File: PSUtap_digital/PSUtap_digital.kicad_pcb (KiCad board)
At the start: 2 copper layers, 179.6 x 181.6 mm, 90 parts, among them J1 USB_B_Micro, J2 ADC_board_SPI, J3 SD_card_SPI, J4 Screen_SPI, SW1 Up, SW2 Down, SW3 Left, SW4 Right, SW5 B, SW6 A, SW7 SW_DPST_x2, T1 CTX33-3, U1 LT1512, U2 BQ2973, U3 Si6926ADQ, U4 CH340G, U5 ATmega328P-AU, U6 LTC3525-5, Y1 12MHz, Y2 16MHz

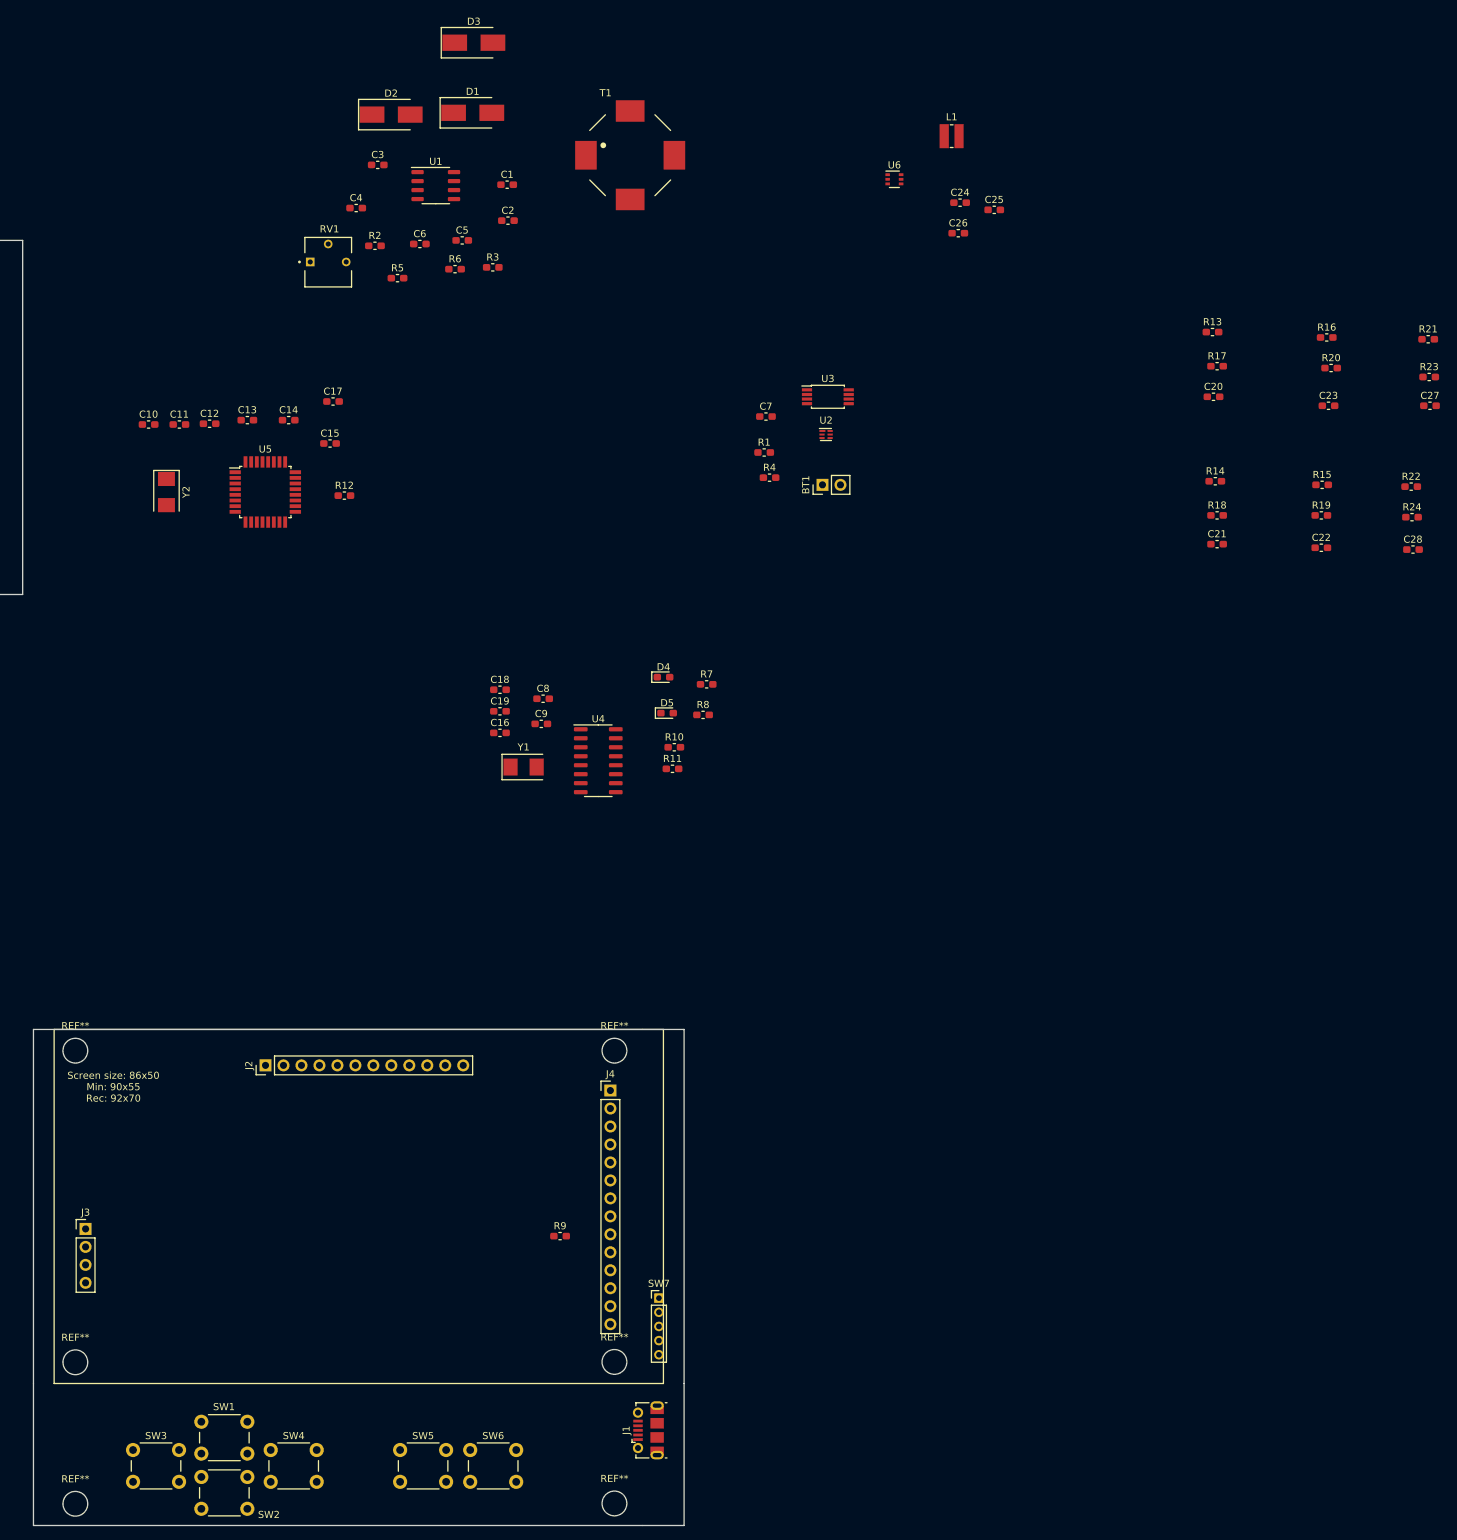
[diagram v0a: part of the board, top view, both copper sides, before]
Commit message: Removed PCB copies, added xtal to ADC in analog board, finished digital board's PCB
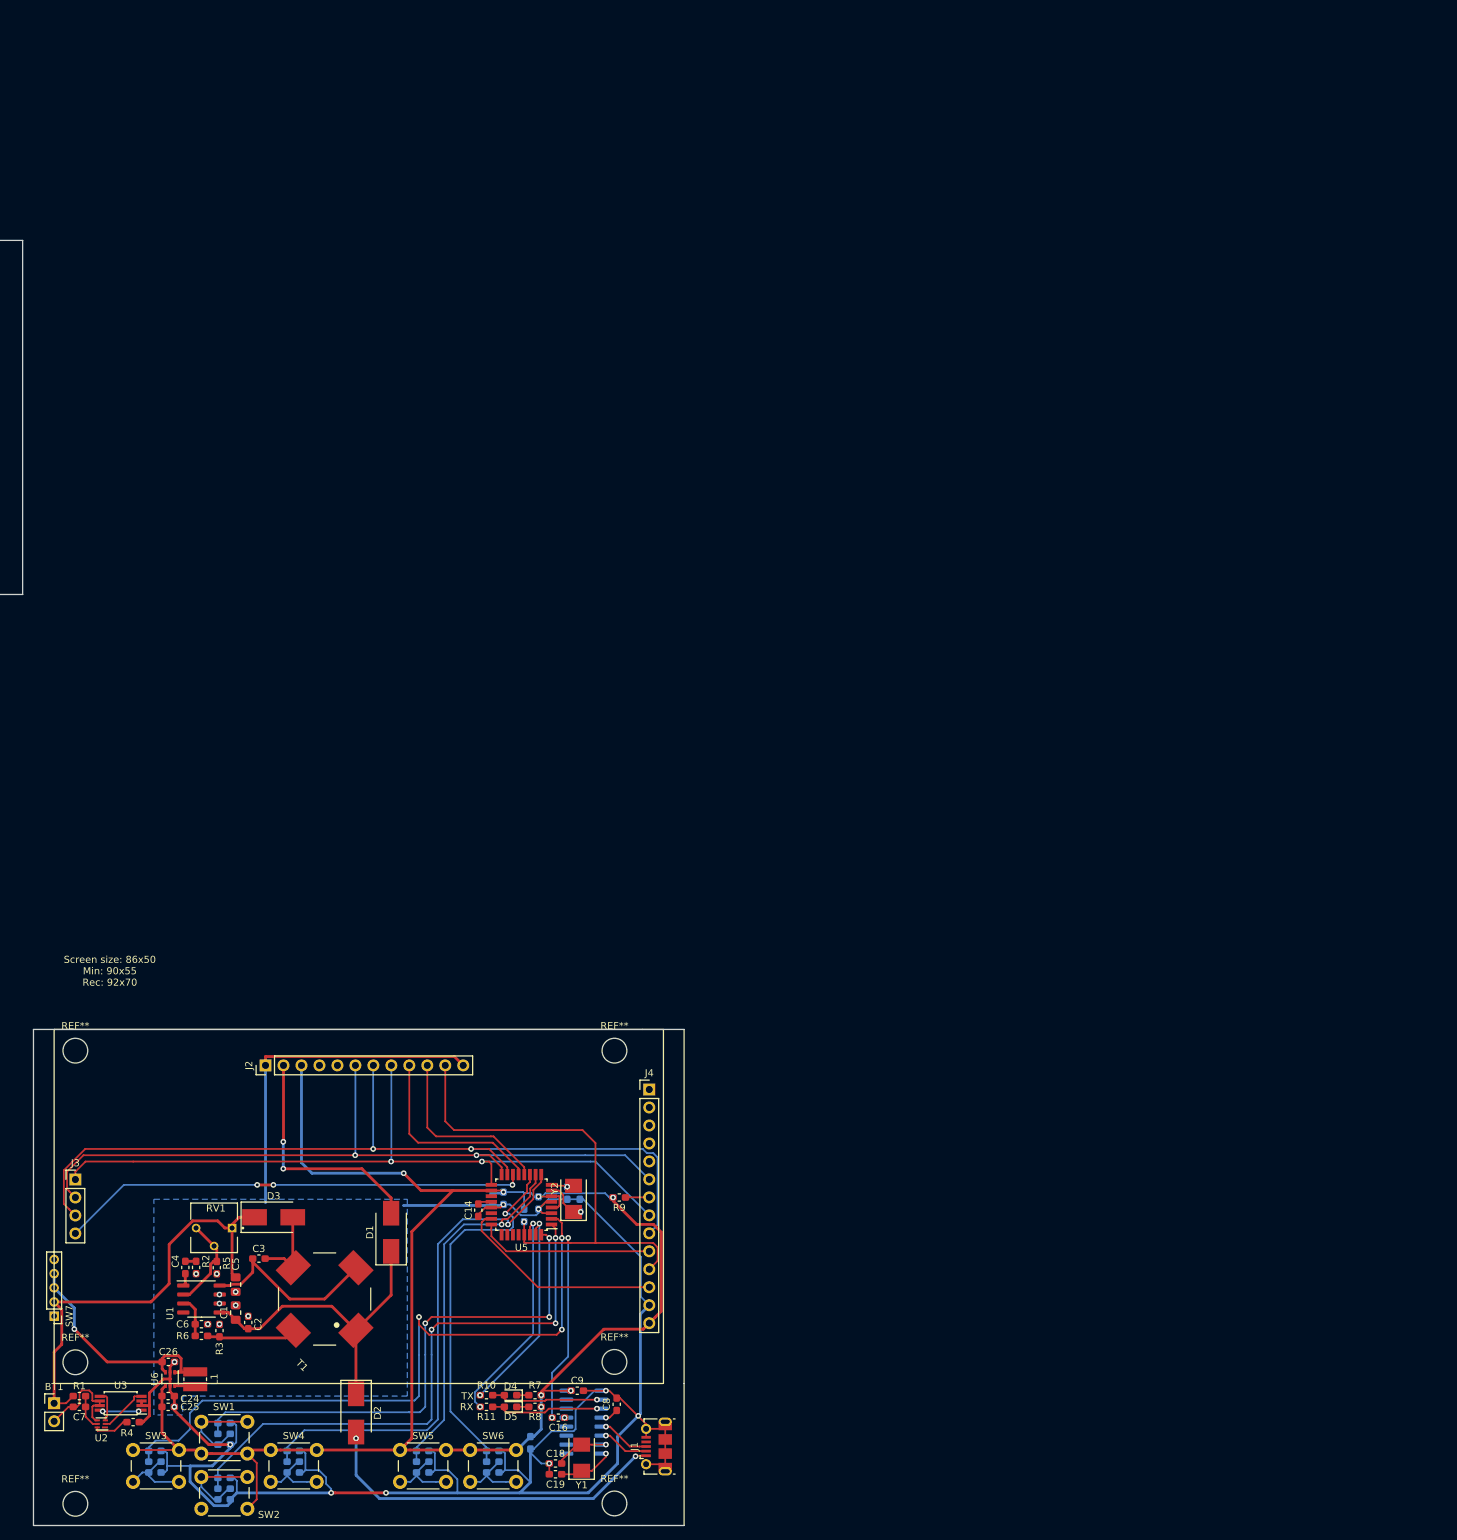
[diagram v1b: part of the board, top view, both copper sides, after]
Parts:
- C1, C5: footprint Capacitor_SMD:C_0603_1608Metric_Pad1.05x0.95mm_HandSolder -> Capacitor_SMD:C_0805_2012Metric_Pad1.15x1.40mm_HandSolder
- C10, C11, C12, C13, C15, C17, C20, C21, C22, C23, C27, C28, R12, R13, R14, R15, R16, R17, R18, R19, R20, R21, R22, R23, R24, U4: moved to B.Cu
- moved R16 215.8 mm to (146.7, 123.8)
- moved R15 215.1 mm to (127.1, 123.8)
- moved R20 214.2 mm to (146.7, 125.3)
- moved R19 213.2 mm to (127.1, 125.3)
- moved R21 213.0 mm to (165.0, 123.8)
- moved R23 210.2 mm to (165.0, 125.3)
- moved R13 209.2 mm to (136.9, 119.9)
- moved C22 208.5 mm to (127.1, 122.3)
- moved C23 207.9 mm to (146.7, 122.3)
- moved R17 207.2 mm to (136.9, 121.4)
- moved L1 205.6 mm to (132.8, 112.2), turned to 270 degrees
- moved C25 205.5 mm to (129.0, 116.1)
- moved C27 205.1 mm to (165.0, 122.3)
- moved C24 202.4 mm to (129.0, 114.6)
- moved C20 201.5 mm to (136.9, 118.4)
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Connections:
- SW7 pad 1: /Vbatt -> (no net)
- SW7 pad 2: Net-(C26-Pad1) -> /Vbatt
- SW7 pad 3: (no net) -> Net-(C26-Pad1)
- SW7 pad 4: (no net) -> Net-(C26-Pad1)
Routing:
- net GND: track 0.00 -> 326.5 mm, vias 0 -> 19
- net /5Vsup: track 0.00 -> 239.5 mm, vias 0 -> 7
- net /MOSI: track 0.00 -> 123.0 mm, vias 0 -> 2
- net /MISO: track 0.00 -> 106.8 mm, vias 0 -> 2
- net /SCLK: track 0.00 -> 104.0 mm, vias 0 -> 2
- net /uC_RESET: track 0.00 -> 97.4 mm, vias 0 -> 3
- net /L: track 0.00 -> 94.6 mm, vias 0 -> 3
- net /D: track 0.00 -> 80.7 mm, vias 0 -> 3
- net /U: track 0.00 -> 74.4 mm, vias 0 -> 3
- net /R: track 0.00 -> 70.7 mm, vias 0 -> 1
- net /SS3: track 0.00 -> 66.1 mm, vias 0 -> 3
- net /Vbatt: track 0.00 -> 63.2 mm
- net /A: track 0.00 -> 52.3 mm, vias 0 -> 1
- net /B: track 0.00 -> 51.0 mm, vias 0 -> 1
- net Net-(D2-Pad2): track 0.00 -> 50.1 mm, vias 0 -> 2
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- added copper zone on B.Cu, net GND
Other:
- board text added: "RX"
- board text added: "TX"

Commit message: Updated PCBs to not have vias on component pads
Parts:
- moved C16 0.64 mm to (184.8, 117.6)
- moved C11 0.52 mm to (180.8, 87.1)
- moved R12 0.27 mm to (179.3, 89.3)
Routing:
- net GND: track 326.5 -> 346.9 mm, vias 19 -> 17
- net /5Vsup: track 239.5 -> 257.1 mm
- net /uC_RESET: track 97.4 -> 104.9 mm
- net Net-(C17-Pad1): track 3.17 -> 7.25 mm
- net Net-(C15-Pad1): track 5.06 -> 9.10 mm
- net Net-(C18-Pad1): track 7.63 -> 10.6 mm
- net Net-(C16-Pad2): track 0.00 -> 2.92 mm
- net Net-(C19-Pad1): track 7.73 -> 10.4 mm
- net Net-(C8-Pad1): track 1.94 -> 3.53 mm
- net Net-(D5-Pad2): track 15.6 -> 17.1 mm
- net Net-(C26-Pad1): track 34.1 -> 35.5 mm
- net Net-(U2-Pad3): track 4.45 -> 5.67 mm
- net /RX: track 31.4 -> 32.5 mm
- net Net-(U3-Pad1): track 5.08 -> 6.04 mm
- net Net-(D2-Pad2): track 50.1 -> 51.0 mm
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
